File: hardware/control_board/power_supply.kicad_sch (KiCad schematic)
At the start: 26 parts, among them J4 6.5/2mm, SW2 Power, U2 LMR38010SDDAR, U3 TLV76133DCYR

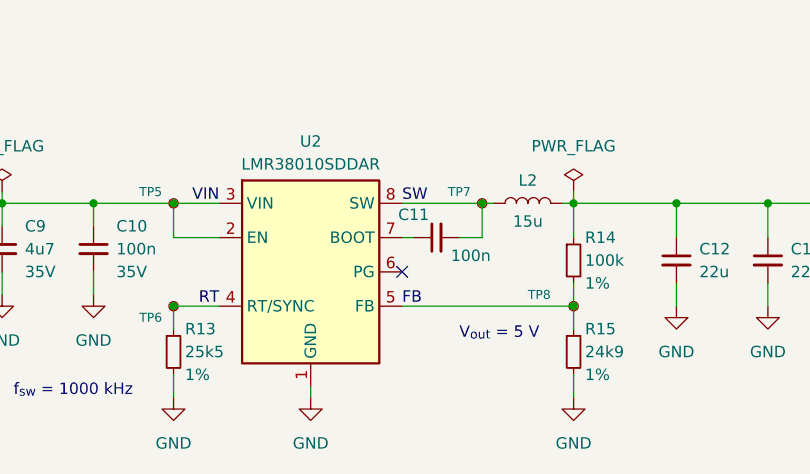
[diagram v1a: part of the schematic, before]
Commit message: Change the buzzer
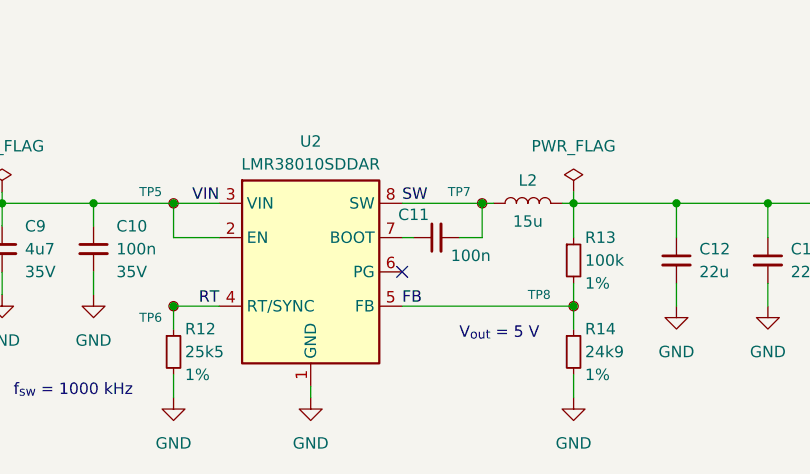
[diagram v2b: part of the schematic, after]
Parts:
- renumbered R13 to R12, R14 to R13, R15 to R14
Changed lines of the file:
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@@
   (symbol (lib_id "Device:R_Small") (at 99.06 115.57 0) (unit 1)
     (in_bom yes) (on_board yes) (dnp no)
-    (property "Reference" "R13" (at 100.33 113.03 0)
+    (property "Reference" "R12" (at 100.33 113.03 0)
       (effects (font (size 1.27 1.27)) (justify left))
     )
@@
       (project "control_board"
         (path "/b652b05a-4e3d-4ad1-b032-18886abe7d45/6b868c6a-e629-4d3b-add8-74bb26b34401"
-          (reference "R13") (unit 1)
+          (reference "R12") (unit 1)
         )
       )
@@
   (symbol (lib_id "Device:R_Small") (at 143.51 105.41 0) (unit 1)
     (in_bom yes) (on_board yes) (dnp no)
-    (property "Reference" "R14" (at 144.78 102.87 0)
+    (property "Reference" "R13" (at 144.78 102.87 0)
       (effects (font (size 1.27 1.27)) (justify left))
     )
@@
       (project "control_board"
         (path "/b652b05a-4e3d-4ad1-b032-18886abe7d45/6b868c6a-e629-4d3b-add8-74bb26b34401"
-          (reference "R14") (unit 1)
+          (reference "R13") (unit 1)
         )
       )
@@
   (symbol (lib_id "Device:R_Small") (at 143.51 115.57 0) (unit 1)
     (in_bom yes) (on_board yes) (dnp no)
-    (property "Reference" "R15" (at 144.78 113.03 0)
+    (property "Reference" "R14" (at 144.78 113.03 0)
       (effects (font (size 1.27 1.27)) (justify left))
     )
@@
       (project "control_board"
         (path "/b652b05a-4e3d-4ad1-b032-18886abe7d45/6b868c6a-e629-4d3b-add8-74bb26b34401"
-          (reference "R15") (unit 1)
-        )
-      )
+          (reference "R14") (unit 1)
+        )
+      )

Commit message: Swap the left and right button signals
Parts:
- SW2: now left out of the parts list
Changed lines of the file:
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@@
   )
   (symbol (lib_id "Switch:SW_SPST") (at 99.06 59.69 0) (unit 1)
-    (in_bom yes) (on_board yes) (dnp no)
+    (in_bom no) (on_board yes) (dnp no)
     (property "Reference" "SW2" (at 99.06 53.34 0)
       (effects (font (size 1.27 1.27)))
